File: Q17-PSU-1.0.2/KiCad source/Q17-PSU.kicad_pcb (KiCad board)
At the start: 2 copper layers, 102 x 102 mm, 36 parts, among them J1-1 AC1-1, J1-2 AC1-2, J1-3 AC2-1, J1-4 AC2-2, J2-1 V+, J2-2 V+, J2-3 GNDPWR, J2-4 GNDPWR, J2-5 GNDPWR, J2-6 V-, J2-7 V-

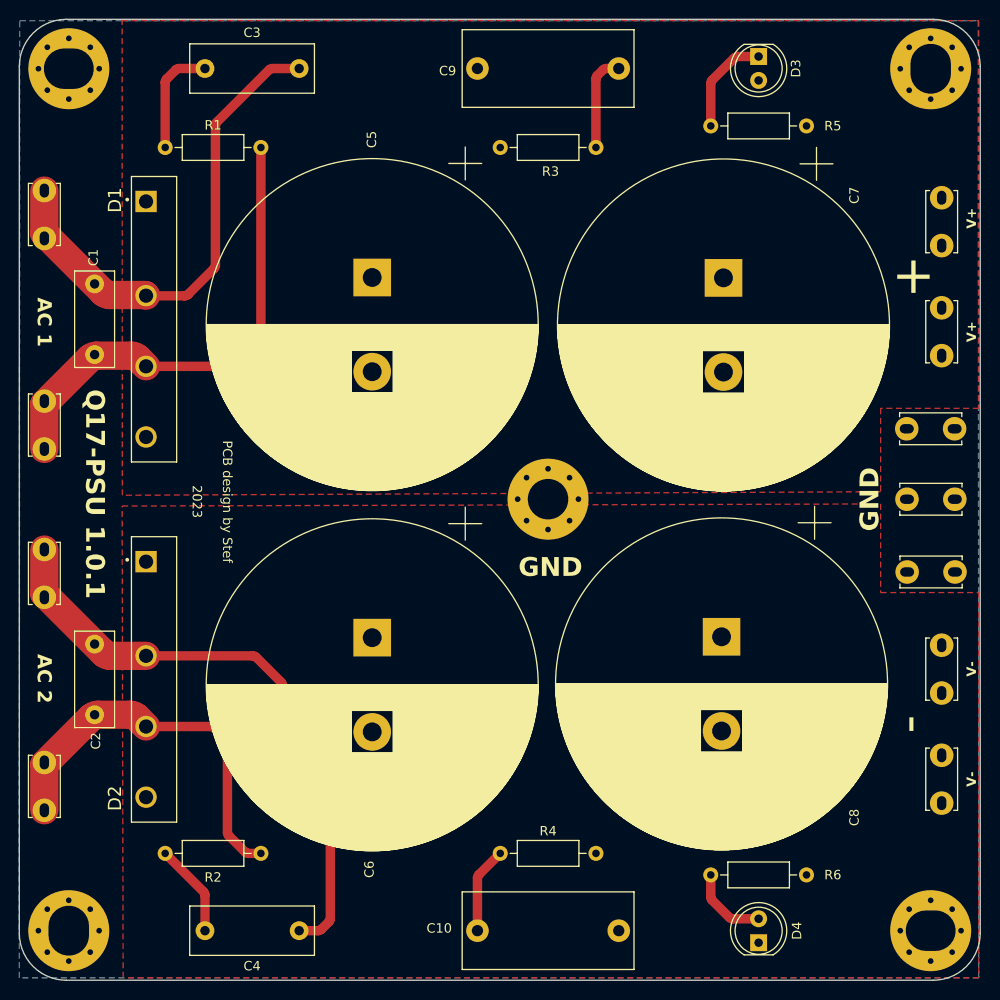
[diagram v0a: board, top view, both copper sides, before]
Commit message: Update PSU files to 1.0.2
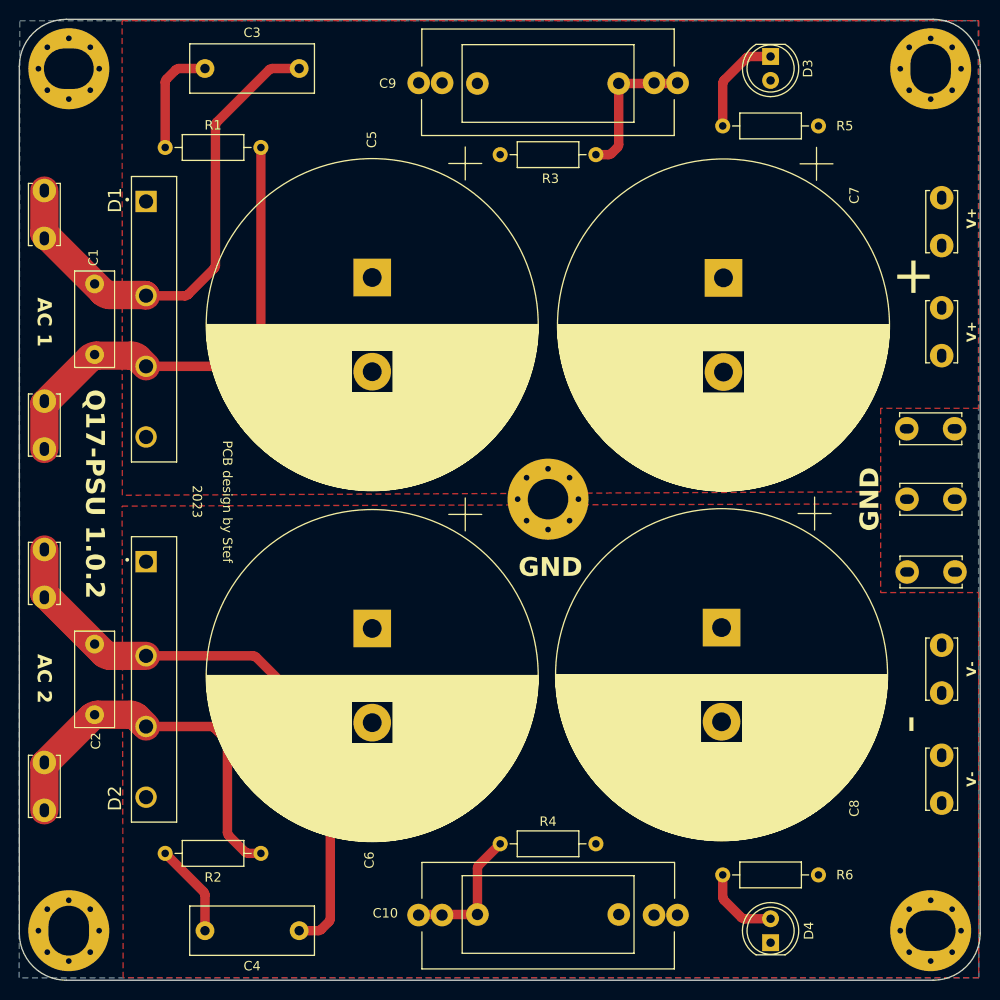
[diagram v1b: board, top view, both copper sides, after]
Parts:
- C10, C9: footprint Capacitor_THT:C_Rect_L18.0mm_W8.0mm_P15.00mm_FKS3_FKP3 -> Q17_Library:C_Rect_Q17_PSU_L26.50_H11.00_P20.50
- moved C10 4.09 mm to (165.4, 135.1)
- moved C9 4.05 mm to (142.9, 46.7)
- moved D3 1.27 mm to (177.8, 43.9)
- moved D4 1.27 mm to (177.8, 138.0)
- moved R5 1.27 mm to (172.7, 51.3)
- moved R6 1.27 mm to (182.9, 130.8)
- moved R4 1.02 mm to (149.1, 127.5)
- moved C6 0.98 mm to (135.5, 104.6)
- moved C8 0.98 mm to (172.6, 104.6)
- moved R3 0.76 mm to (159.3, 54.4)
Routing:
- net Net-(C10-Pad2): track 9.18 -> 14.7 mm
- net Net-(C9-Pad2): track 10.2 -> 15.6 mm
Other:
- board text added: "Q17-PSU 1.0.2"
- board text removed: "Q17-PSU 1.0.1"
